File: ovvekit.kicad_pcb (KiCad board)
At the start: 4 copper layers, 75 x 76 mm, 102 parts, among them IC1 MAX4466EXK+T, J1 ESP_PROG_JTAG, J2 ESP_PROG_UART, J201 Power_Planes, Q201 Q_PMOS_GSD, SW1 SW_Push, SW2 SW_Push, SW3 SW_Push, U1 ESP32-WROOM-32

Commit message: Now amplifier is in local lib, hopefully.
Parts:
- removed the svg2mod at (13.5, 1.00)
- IC1: footprint SamacSys_Parts:SOT65P210X110-5N -> Special_Parts:SOT65P210X110-5N
- MK1: footprint Special_Parts:CMEJ062742P -> SamacSys_Parts:CMEJ062742P

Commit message: Now all footprint are updated to. SamacSys is no longer a dependency of this project.
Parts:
- MK1: footprint SamacSys_Parts:CMEJ062742P -> Special_Parts:CMEJ062742P
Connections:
- DN1 pad 4: (no net) -> Net-(DN1-Pad4)
- DN27 pad 2: (no net) -> Net-(DN27-Pad2)
- J1 pad 10: (no net) -> Net-(J1-Pad10)
- U1 pad 17: (no net) -> Net-(U1-Pad17)
- U1 pad 18: (no net) -> Net-(U1-Pad18)
- U1 pad 19: (no net) -> Net-(U1-Pad19)
- U1 pad 20: (no net) -> Net-(U1-Pad20)
- U1 pad 21: (no net) -> Net-(U1-Pad21)
- U1 pad 22: (no net) -> Net-(U1-Pad22)
- U1 pad 24: (no net) -> Net-(U1-Pad24)
- U1 pad 26: (no net) -> Net-(U1-Pad26)
- U1 pad 27: (no net) -> Net-(U1-Pad27)
- U1 pad 28: (no net) -> Net-(U1-Pad28)
- U1 pad 29: (no net) -> Net-(U1-Pad29)
- U1 pad 30: (no net) -> Net-(U1-Pad30)
- U1 pad 31: (no net) -> Net-(U1-Pad31)
- U1 pad 32: (no net) -> Net-(U1-Pad32)
- U1 pad 33: (no net) -> Net-(U1-Pad33)
- U1 pad 36: (no net) -> Net-(U1-Pad36)
- U1 pad 37: (no net) -> Net-(U1-Pad37)
- U1 pad 4: (no net) -> Net-(U1-Pad4)
- U1 pad 5: (no net) -> Net-(U1-Pad5)
- U1 pad 6: (no net) -> Net-(U1-Pad6)
- U1 pad 7: (no net) -> Net-(U1-Pad7)
- U1 pad 8: (no net) -> Net-(U1-Pad8)

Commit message: Added a LDO, maybe not the final one but there is one on the PCB now. Added a voltage divider for measureing battery voltage.
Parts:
- added R201: 1M, Resistor_SMD:R_0603_1608Metric_Pad0.98x0.95mm_HandSolder, B.Cu at (26.7, 11.4)
- added R202: 1M, Resistor_SMD:R_0603_1608Metric_Pad0.98x0.95mm_HandSolder, B.Cu at (24.1, 11.4)
- added U201: TLV75733PDRV, Package_SON:WSON-6-1EP_2x2mm_P0.65mm_EP1x1.6mm, B.Cu at (34.3, 21.6)
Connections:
- U1 pad 6: Net-(U1-Pad6) -> Battery_monitor
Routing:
- net VCC: track 132.8 -> 146.1 mm
- net GND: track 204.5 -> 211.9 mm
- net Battery_monitor: track 0.00 -> 6.64 mm
- net +3V3: track 126.9 -> 130.2 mm

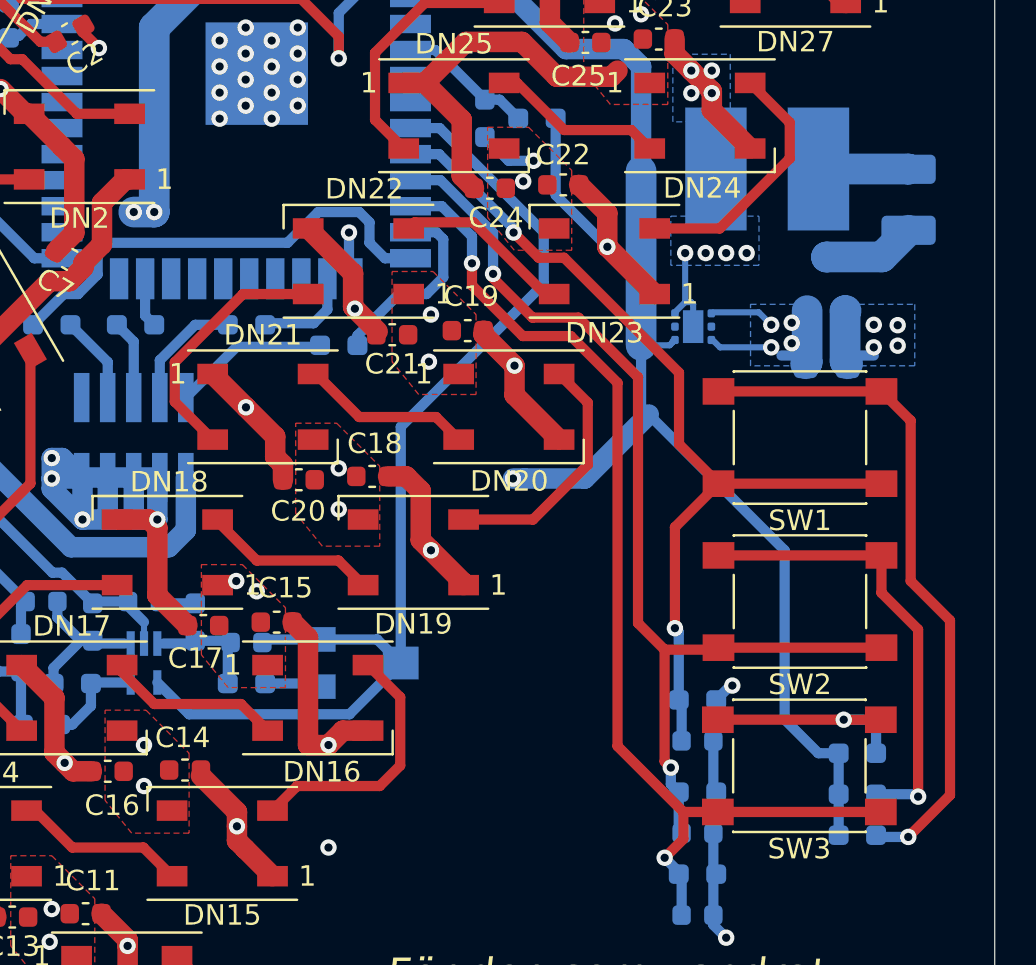
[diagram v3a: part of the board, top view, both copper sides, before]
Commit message: Added some 1206 caps to be large stabilizing capacitors. Added a rank 1 RC filter to audio out, with a bypass solderbridge if wanted.
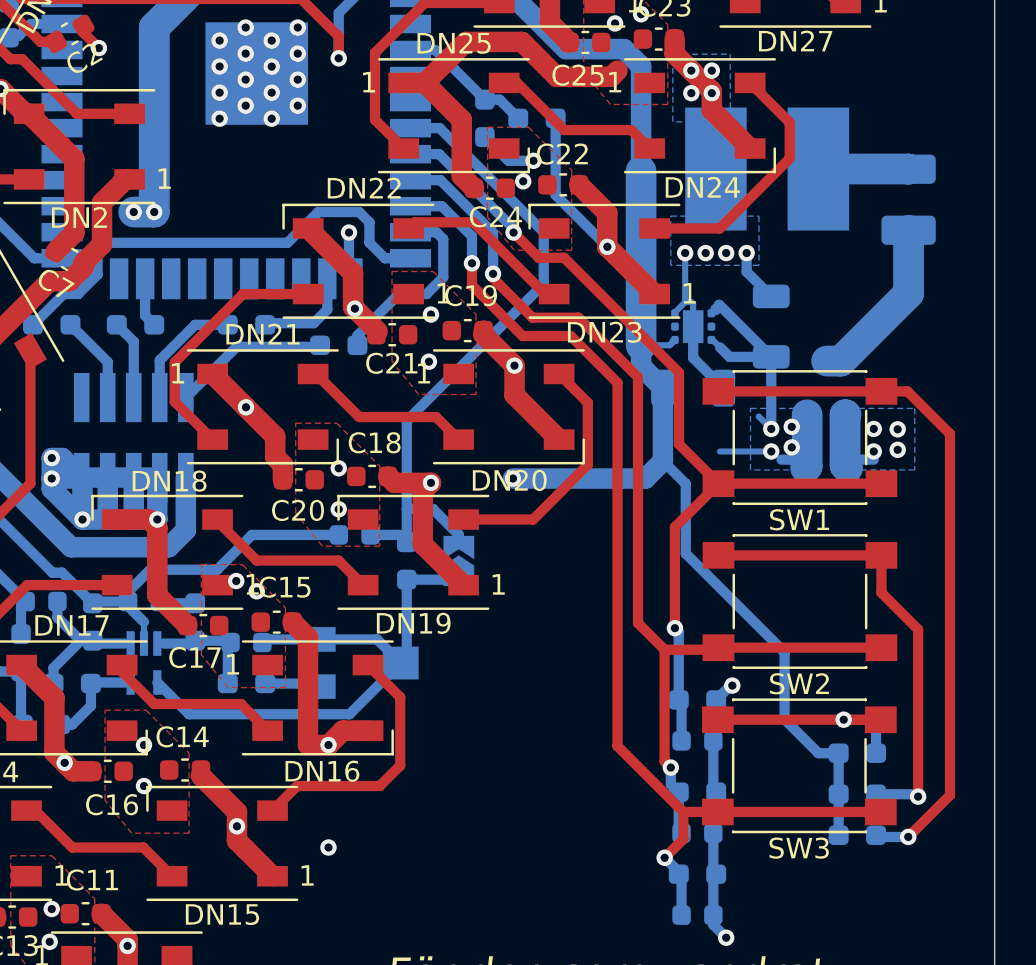
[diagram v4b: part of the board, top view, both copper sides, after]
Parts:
- added C201: 10uF, Capacitor_SMD:C_1206_3216Metric, B.Cu at (38.1, 21.6)
- added C202: 10uF, Capacitor_SMD:C_1206_3216Metric, B.Cu at (34.3, 24.6)
- added C31: 0.1uF, Capacitor_SMD:C_0603_1608Metric, B.Cu at (17.8, 31.8)
- added JP10: Jumper_2_Bridged, Jumper:SolderJumper-2_P1.3mm_Open_TrianglePad1.0x1.5mm, B.Cu at (22.9, 33.0)
- added R13: 100, Resistor_SMD:R_0603_1608Metric_Pad0.98x0.95mm_HandSolder, B.Cu at (20.3, 33.0)
- moved D201 5.08 mm to (40.8, 28.5)
- moved Q201 5.08 mm to (40.8, 24.6)
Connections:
- C30 pad 1: AUDIO_OUT -> Net-(C30-Pad1)
- IC1 pad 4: AUDIO_OUT -> Net-(C30-Pad1)
- RV1 pad 2: AUDIO_OUT -> Net-(C30-Pad1)
- RV1 pad 3: AUDIO_OUT -> Net-(C30-Pad1)
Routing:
- net Net-(C30-Pad1): track 0.00 -> 27.6 mm
- net AUDIO_OUT: track 53.4 -> 31.9 mm
- net GNDA: track 26.9 -> 38.8 mm
- net VCC: track 146.1 -> 155.3 mm
- net GND: track 211.9 -> 218.2 mm
- net Net-(F201-Pad2): track 4.55 -> 8.45 mm
- net Net-(R101-Pad2): track 33.5 -> 34.3 mm

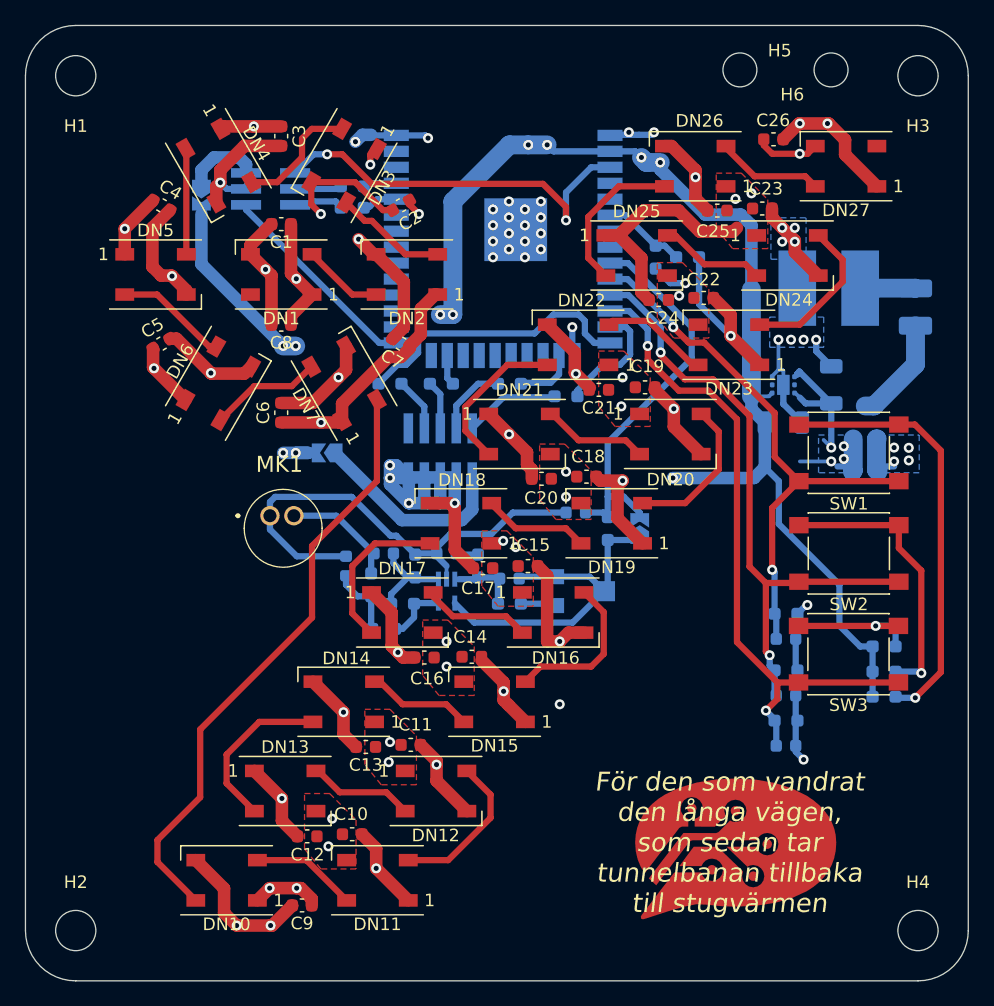
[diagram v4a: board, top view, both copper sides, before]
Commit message: Added some primitive filter for 3V3A and GNDA. Added the IMU to the board.
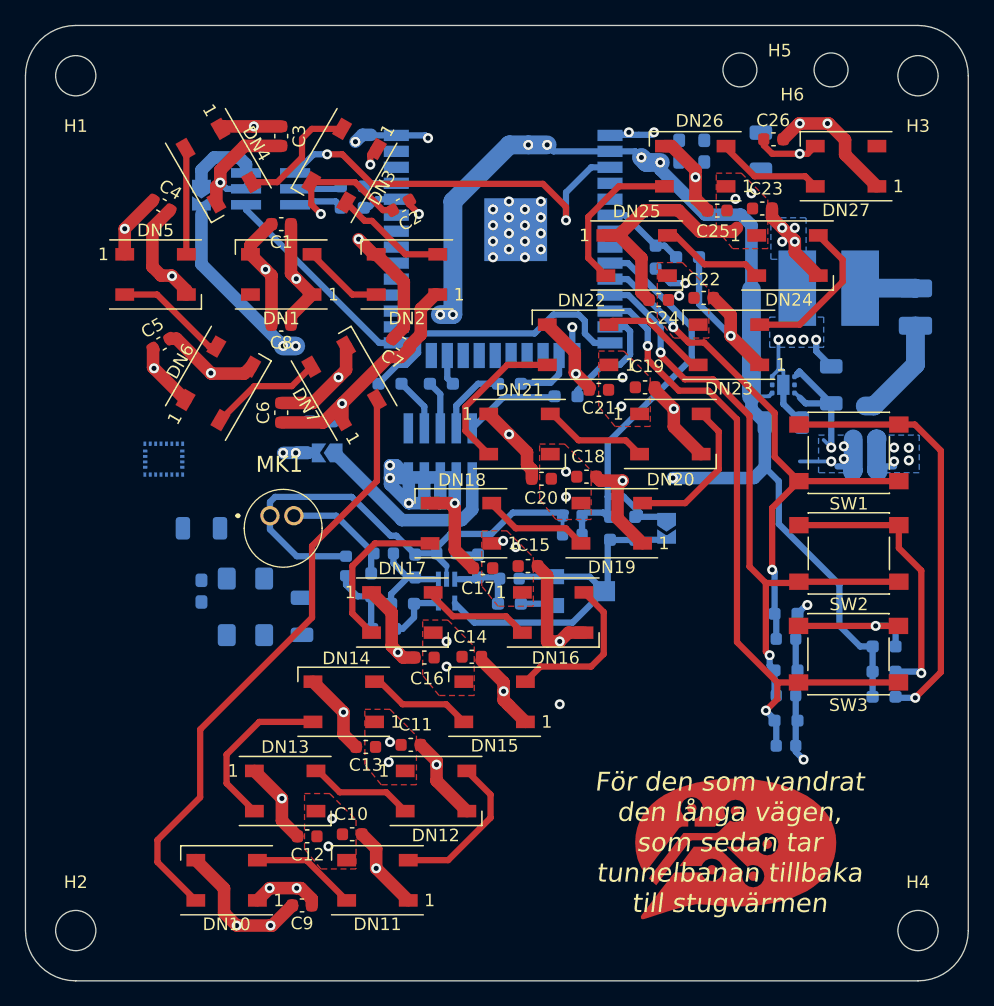
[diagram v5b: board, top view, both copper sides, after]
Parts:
- removed C31: 0.1uF, Capacitor_SMD:C_0603_1608Metric
- removed JP10: Jumper_2_Bridged, Jumper:SolderJumper-2_P1.3mm_Open_TrianglePad1.0x1.5mm
- removed R13: 100, Resistor_SMD:R_0603_1608Metric_Pad0.98x0.95mm_HandSolder
- added AC1: LSM9DS1TR, Special_Parts:LGA-24L_3X3.5X1MM_, B.Cu at (-15.0, 27.5)
- added C203: 10uF, Capacitor_SMD:C_1206_3216Metric, B.Cu at (32.5, 3.00)
- added C204: 100n, Capacitor_SMD:C_0603_1608Metric_Pad1.08x0.95mm_HandSolder, B.Cu at (-2.50, 24.5)
- added C205: 100n, Capacitor_SMD:C_0603_1608Metric_Pad1.08x0.95mm_HandSolder, B.Cu at (28.0, 3.00)
- added C206: 100n, Capacitor_SMD:C_0603_1608Metric_Pad1.08x0.95mm_HandSolder, B.Cu at (-12.0, 38.0)
- added C207: 100n, Capacitor_SMD:C_0603_1608Metric_Pad1.08x0.95mm_HandSolder, B.Cu at (26.0, 3.00)
- added C208: 10uF, Capacitor_SMD:C_1206_3216Metric, B.Cu at (-4.00, 40.0)
- added C209: 10uF, Capacitor_SMD:C_1206_3216Metric, B.Cu at (-12.0, 33.0)
- added C310: 100n, Capacitor_SMD:C_0603_1608Metric, B.Cu at (17.5, 32.0)
- added C311: 100n, Capacitor_SMD:C_0603_1608Metric, B.Cu at (17.5, 33.5)
- added JP300: Jumper_2_Bridged, Jumper:SolderJumper-2_P1.3mm_Open_TrianglePad1.0x1.5mm, B.Cu at (25.0, 33.0)
- added L201: L, Inductor_SMD:L_1206_3216Metric_Pad1.42x1.75mm_HandSolder, B.Cu at (-8.50, 41.5)
- added L202: L, Inductor_SMD:L_1206_3216Metric_Pad1.42x1.75mm_HandSolder, B.Cu at (-8.50, 37.0)
- added R310: 1k, Resistor_SMD:R_0603_1608Metric_Pad0.98x0.95mm_HandSolder, B.Cu at (20.5, 33.0)
- added R311: 1k, Resistor_SMD:R_0603_1608Metric_Pad0.98x0.95mm_HandSolder, B.Cu at (22.5, 33.0)
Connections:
- DN1 pad 4: Net-(DN1-Pad4) -> (no net)
- DN27 pad 2: Net-(DN27-Pad2) -> (no net)
- J1 pad 10: Net-(J1-Pad10) -> (no net)
- U1 pad 17: Net-(U1-Pad17) -> (no net)
- U1 pad 18: Net-(U1-Pad18) -> (no net)
- U1 pad 19: Net-(U1-Pad19) -> (no net)
- U1 pad 20: Net-(U1-Pad20) -> (no net)
- U1 pad 21: Net-(U1-Pad21) -> (no net)
- U1 pad 22: Net-(U1-Pad22) -> (no net)
- U1 pad 24: Net-(U1-Pad24) -> (no net)
- U1 pad 26: Net-(U1-Pad26) -> (no net)
- U1 pad 27: Net-(U1-Pad27) -> (no net)
- U1 pad 28: Net-(U1-Pad28) -> (no net)
- U1 pad 29: Net-(U1-Pad29) -> (no net)
- U1 pad 30: Net-(U1-Pad30) -> (no net)
- U1 pad 31: Net-(U1-Pad31) -> (no net)
- U1 pad 32: Net-(U1-Pad32) -> (no net)
- U1 pad 33: Net-(U1-Pad33) -> (no net)
- U1 pad 36: Net-(U1-Pad36) -> (no net)
- U1 pad 37: Net-(U1-Pad37) -> (no net)
- U1 pad 4: Net-(U1-Pad4) -> (no net)
- U1 pad 5: Net-(U1-Pad5) -> (no net)
- U1 pad 7: Net-(U1-Pad7) -> (no net)
- U1 pad 8: Net-(U1-Pad8) -> (no net)
- U201 pad 2: Net-(U201-Pad2) -> (no net)
- U201 pad 5: Net-(U201-Pad5) -> (no net)
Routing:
- net AUDIO_OUT: track 31.9 -> 35.9 mm
- net Net-(C30-Pad1): track 27.6 -> 30.0 mm
- net VCC: track 155.3 -> 157.2 mm
- net GNDA: track 38.8 -> 40.3 mm

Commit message: Added more filtering. Placed bypass caps near esp32 power intake.
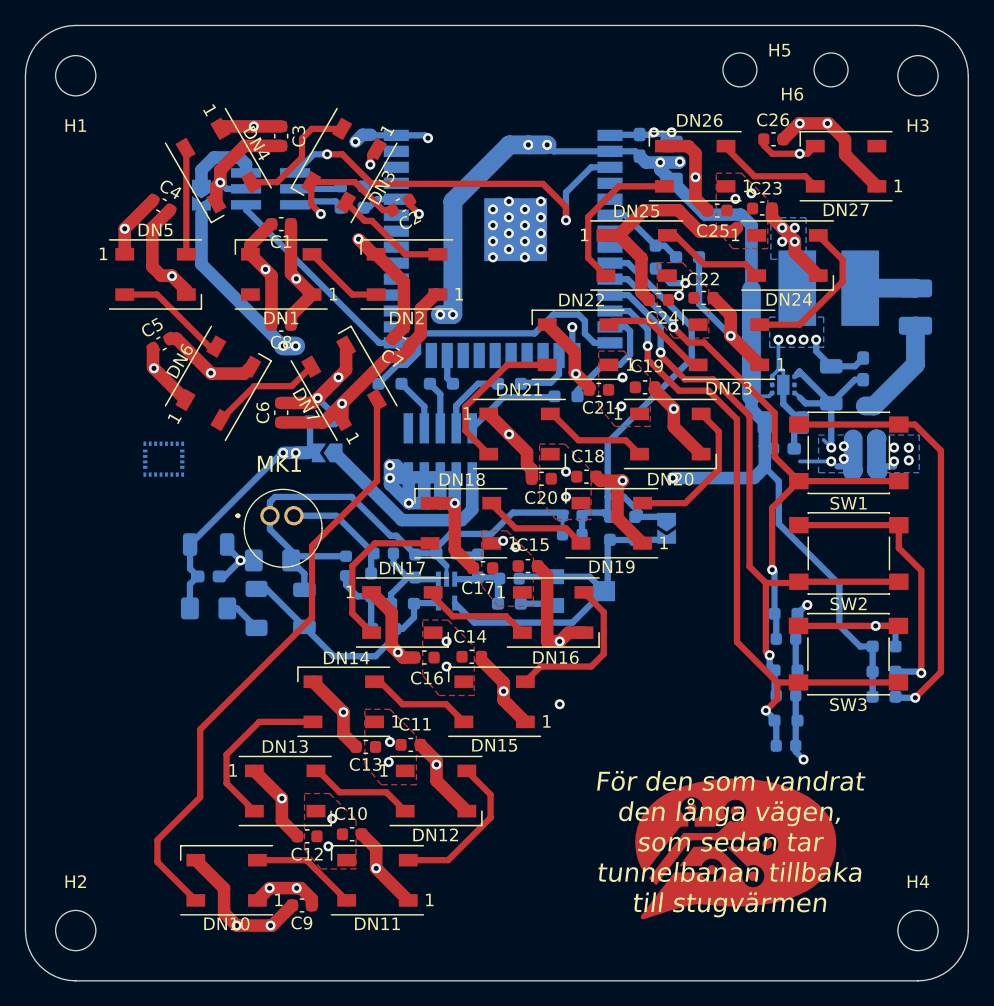
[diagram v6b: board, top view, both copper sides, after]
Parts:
- added C210: 100n, Capacitor_SMD:C_0603_1608Metric_Pad1.08x0.95mm_HandSolder, B.Cu at (40.6, 20.3)
- added R210: 10, Resistor_SMD:R_1206_3216Metric_Pad1.30x1.75mm_HandSolder, B.Cu at (-7.62, 39.4)
- moved C205 24.5 mm to (34.3, 26.7), turned to 0 degrees
- moved C203 7.15 mm to (25.4, 3.81)
- moved L201 3.62 mm to (-11.4, 39.4)
- moved C207 3.17 mm to (22.9, 2.54)
- moved L202 2.59 mm to (-6.35, 35.6)
- moved C209 1.41 mm to (-11.4, 34.3)
- moved C206 1.30 mm to (-11.4, 36.8), turned to 0 degrees
- moved C208 0.66 mm to (-3.81, 39.4)
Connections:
- AC1 pad 1: (no net) -> Net-(AC1-Pad1)
- AC1 pad 10: (no net) -> Net-(AC1-Pad10)
- AC1 pad 11: (no net) -> Net-(AC1-Pad11)
- AC1 pad 12: (no net) -> Net-(AC1-Pad12)
- AC1 pad 13: (no net) -> Net-(AC1-Pad13)
- AC1 pad 14: (no net) -> Net-(AC1-Pad14)
- AC1 pad 15: (no net) -> Net-(AC1-Pad15)
- AC1 pad 16: (no net) -> Net-(AC1-Pad16)
- AC1 pad 17: (no net) -> Net-(AC1-Pad17)
- AC1 pad 18: (no net) -> Net-(AC1-Pad18)
- AC1 pad 19: (no net) -> Net-(AC1-Pad19)
- AC1 pad 2: (no net) -> Net-(AC1-Pad2)
- AC1 pad 20: (no net) -> Net-(AC1-Pad20)
- AC1 pad 21: (no net) -> Net-(AC1-Pad21)
- AC1 pad 22: (no net) -> Net-(AC1-Pad22)
- AC1 pad 23: (no net) -> Net-(AC1-Pad23)
- AC1 pad 24: (no net) -> Net-(AC1-Pad24)
- AC1 pad 3: (no net) -> Net-(AC1-Pad3)
- AC1 pad 4: (no net) -> Net-(AC1-Pad4)
- AC1 pad 5: (no net) -> Net-(AC1-Pad5)
- AC1 pad 6: (no net) -> Net-(AC1-Pad6)
- AC1 pad 7: (no net) -> Net-(AC1-Pad7)
- AC1 pad 8: (no net) -> Net-(AC1-Pad8)
- AC1 pad 9: (no net) -> Net-(AC1-Pad9)
- C203 pad 1: VCC -> +3V3
- DN1 pad 4: (no net) -> Net-(DN1-Pad4)
- DN27 pad 2: (no net) -> Net-(DN27-Pad2)
- J1 pad 10: (no net) -> Net-(J1-Pad10)
- L201 pad 2: +3.3VA -> Net-(L201-Pad2)
- U1 pad 17: (no net) -> Net-(U1-Pad17)
- U1 pad 18: (no net) -> Net-(U1-Pad18)
- U1 pad 19: (no net) -> Net-(U1-Pad19)
- U1 pad 20: (no net) -> Net-(U1-Pad20)
- U1 pad 21: (no net) -> Net-(U1-Pad21)
- U1 pad 22: (no net) -> Net-(U1-Pad22)
- U1 pad 24: (no net) -> Net-(U1-Pad24)
- U1 pad 26: (no net) -> Net-(U1-Pad26)
- U1 pad 27: (no net) -> Net-(U1-Pad27)
- U1 pad 28: (no net) -> Net-(U1-Pad28)
- U1 pad 29: (no net) -> Net-(U1-Pad29)
- U1 pad 30: (no net) -> Net-(U1-Pad30)
- U1 pad 31: (no net) -> Net-(U1-Pad31)
- U1 pad 32: (no net) -> Net-(U1-Pad32)
- U1 pad 33: (no net) -> Net-(U1-Pad33)
- U1 pad 36: (no net) -> Net-(U1-Pad36)
- U1 pad 37: (no net) -> Net-(U1-Pad37)
- U1 pad 4: (no net) -> Net-(U1-Pad4)
- U1 pad 5: (no net) -> Net-(U1-Pad5)
- U1 pad 7: (no net) -> Net-(U1-Pad7)
- U1 pad 8: (no net) -> Net-(U1-Pad8)
- U201 pad 2: (no net) -> Net-(U201-Pad2)
- U201 pad 5: (no net) -> Net-(U201-Pad5)
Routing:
- net +3V3: track 130.2 -> 151.2 mm
- net GND: track 218.2 -> 233.8 mm, vias 63 -> 65
- net +3.3VA: track 4.92 -> 19.4 mm
- net VCC: track 157.2 -> 160.5 mm
- net Net-(L201-Pad2): track 0.00 -> 2.96 mm
- net GNDA: track 40.3 -> 43.0 mm
